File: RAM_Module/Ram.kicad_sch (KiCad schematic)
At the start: 3 parts, among them SW1 SW_Push, U3 74LS157, U4 74LS00

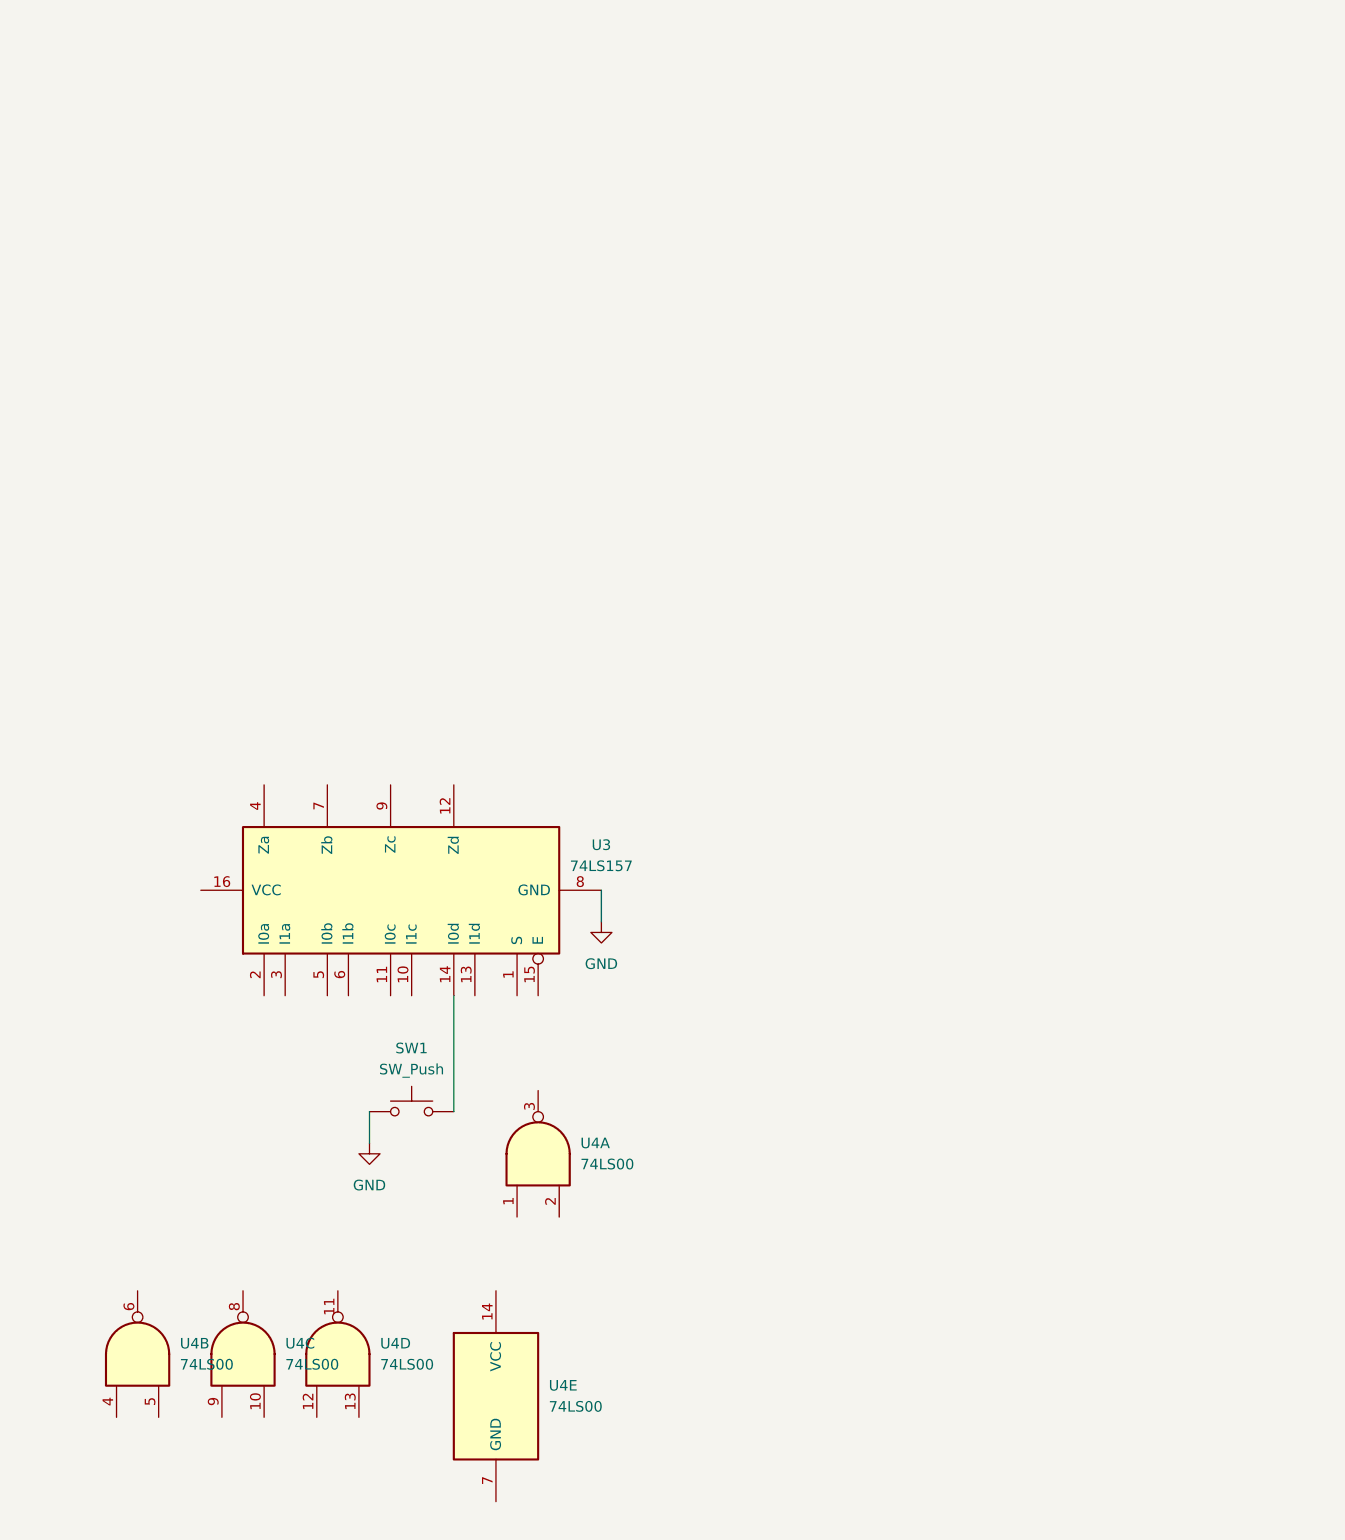
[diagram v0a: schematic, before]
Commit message: added buses for addresses. RAM WIP
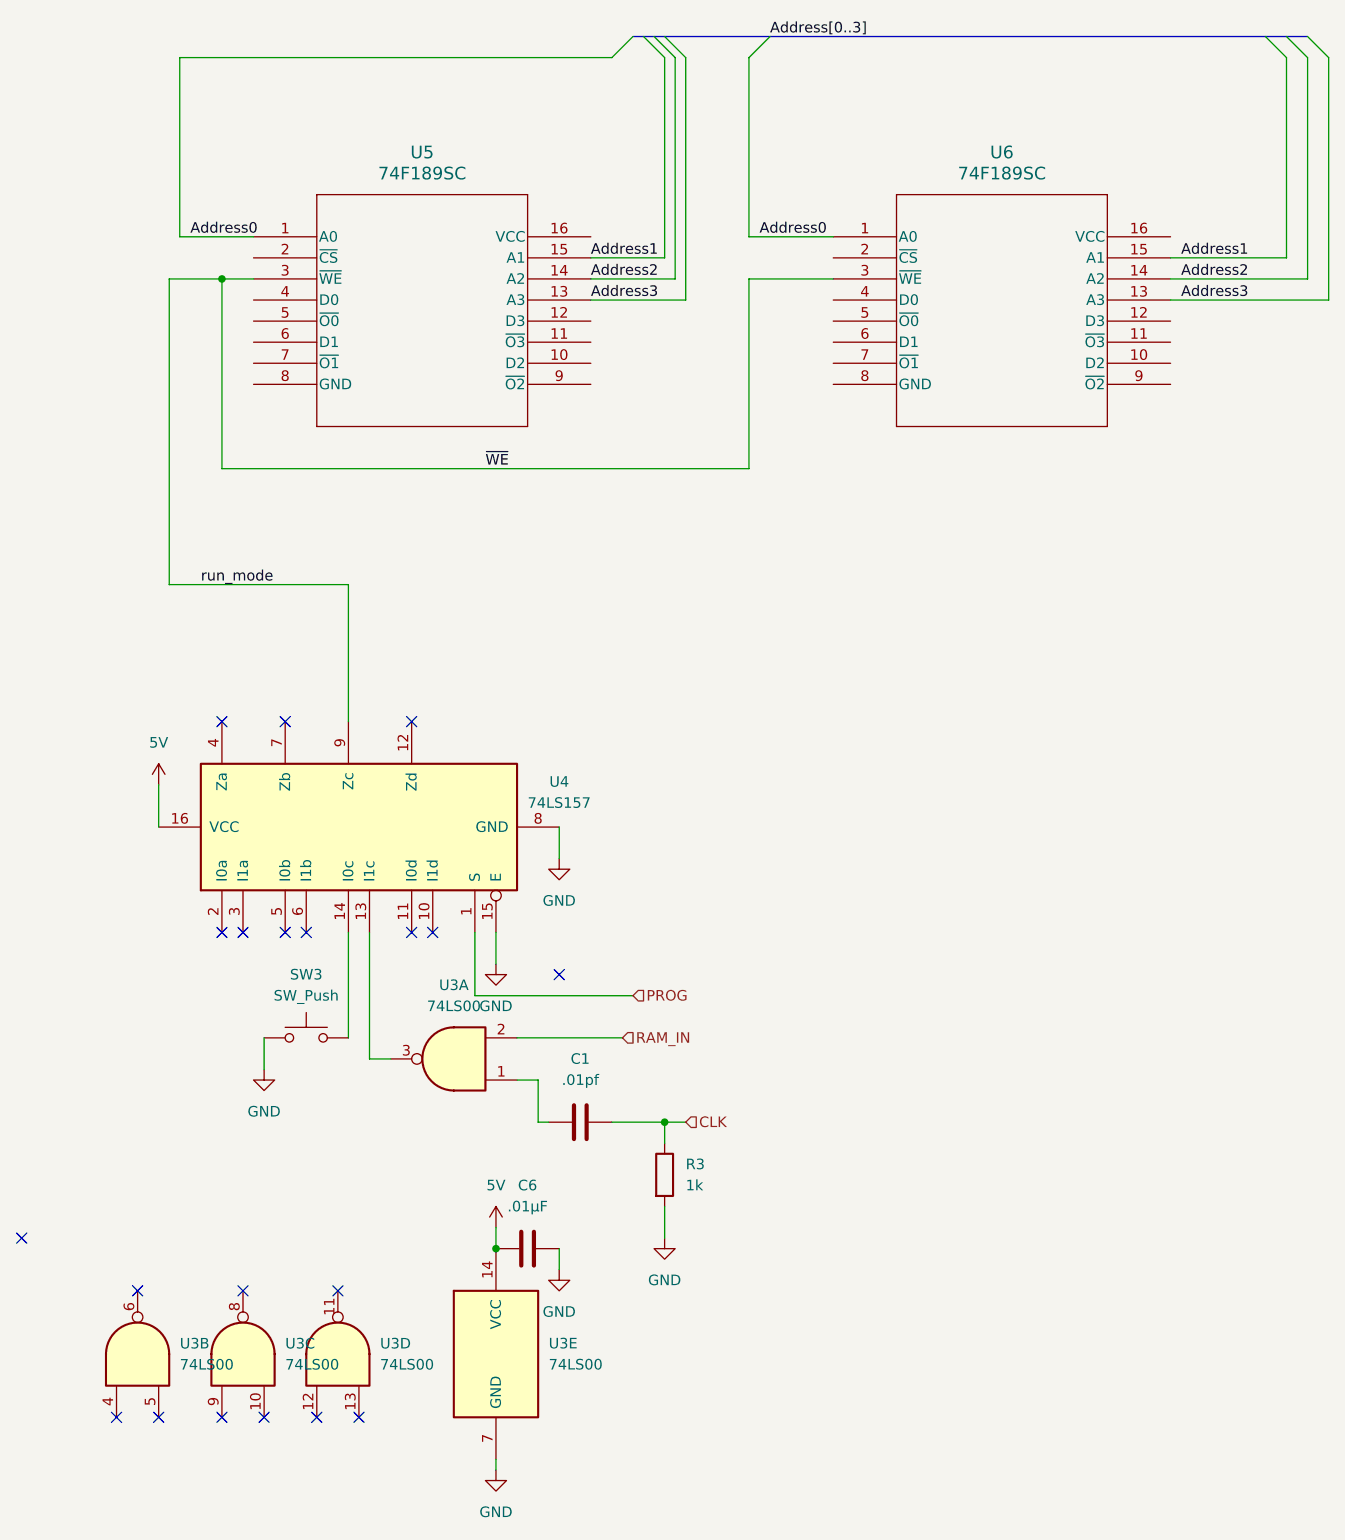
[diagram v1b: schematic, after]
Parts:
- added C1: .01pf, symbol Device:C
- added C6: .01µF, Capacitor_THT:C_Disc_D5.0mm_W2.5mm_P2.50mm, symbol Device:C
- added R3: 1k, symbol Device:R
- added U5, U6: 74F189SC, SOIC16_9P9X3P9_ONS, symbol 74189:74F189SC
- U4: renamed from U3; symbol 74xx:74LS157 -> 74LS157:my_74LS157
- renumbered SW1 to SW3, U4 to U3
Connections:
- net GND: now also U3.7 (GND), U4.15 (E), C6.1, R3.2
- net 5V: now reaches U3.14 (VCC)
- net 5V: now also U4.16 (VCC), C6.2
- net PROG: now reaches U4.1 (S)
- net at U4.13 (I1c): now also U3.3
- net run_mode: now reaches U4.9 (Zc)
- net run_mode: now also U5.3 (~{WE}), U6.3 (~{WE})
- net at U3.1: now also C1.1
- net RAM_IN: now reaches U3.2
- new net Address0: U5.1 (A0), U6.1 (A0)
- new net Address1: U5.15 (A1), U6.15 (A1)
- new net Address2: U5.14 (A2), U6.14 (A2)
- new net Address3: U5.13 (A3), U6.13 (A3)
- new net CLK: C1.2, R3.1
- no-connect marks 0 -> 20
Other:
- moved on the sheet: SW3, U3A, U3E, U4

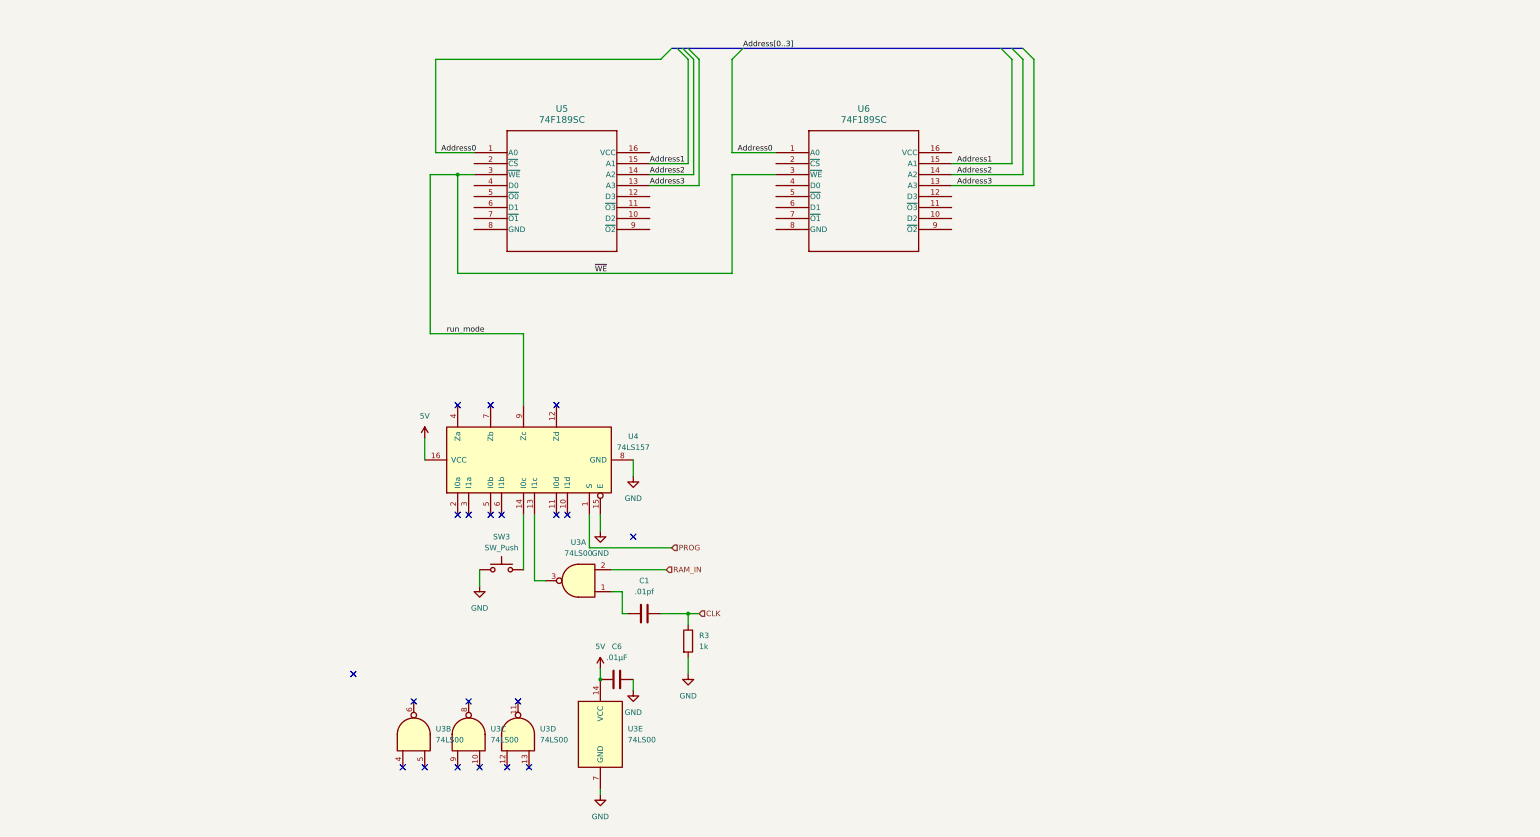
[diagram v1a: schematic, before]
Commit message: connected internal memory
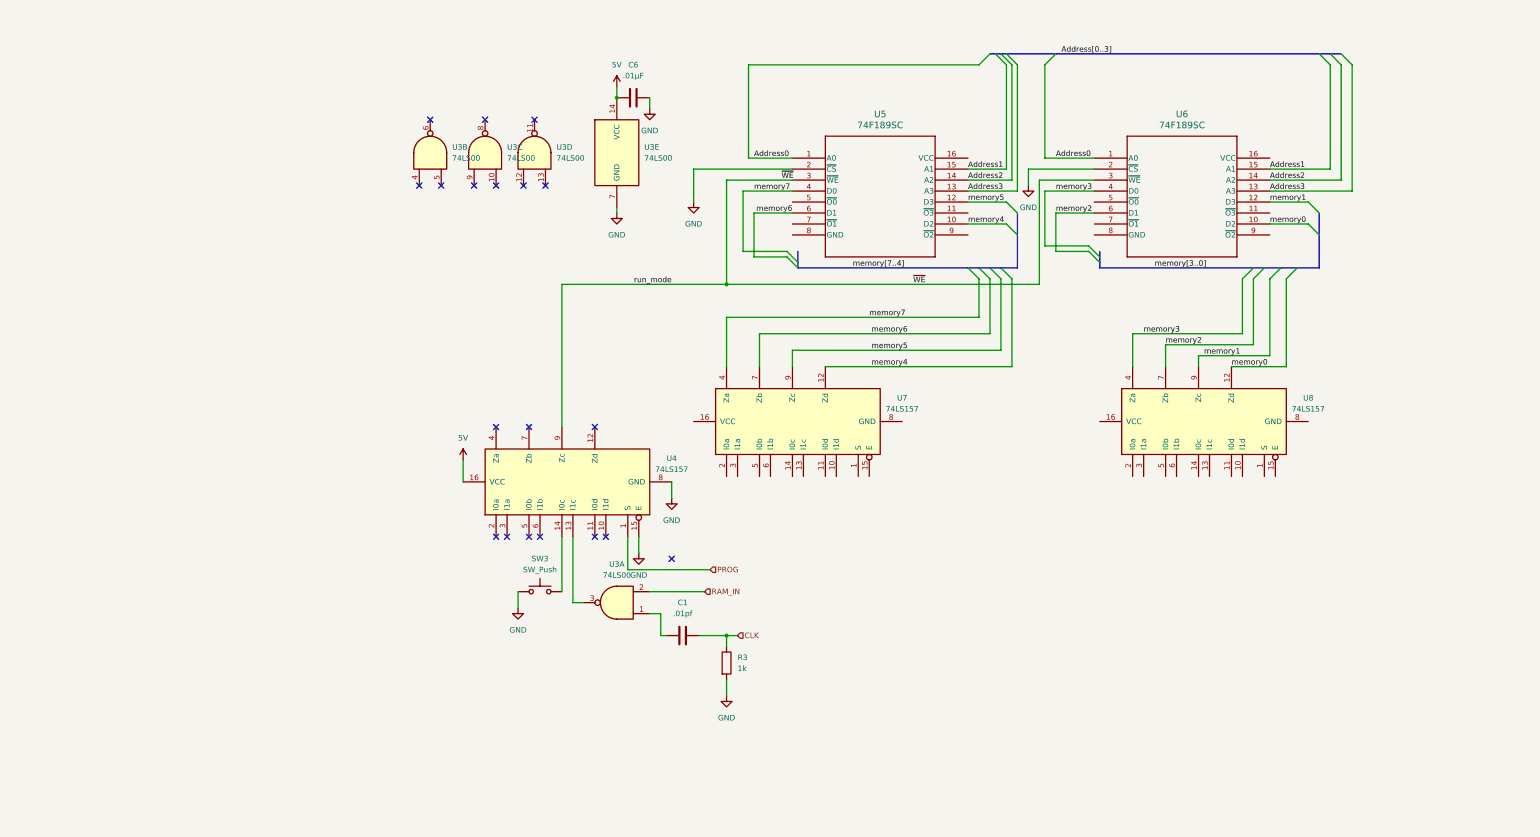
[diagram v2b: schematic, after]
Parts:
- added U7, U8: 74LS157, symbol 74LS157:my_74LS157
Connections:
- net GND: now also U5.2 (~{CS}), U6.2 (~{CS})
- net memory4: now reaches U5.10 (D2)
- net memory4: now also U7.12 (Zd)
- net memory5: now reaches U5.12 (D3)
- net memory5: now also U7.9 (Zc)
- net memory7: now reaches U5.4 (D0)
- net memory7: now also U7.4 (Za)
- net memory6: now reaches U5.6 (D1)
- net memory6: now also U7.7 (Zb)
- net memory0: now reaches U6.10 (D2)
- net memory0: now also U8.12 (Zd)
- net memory1: now reaches U6.12 (D3)
- net memory1: now also U8.9 (Zc)
- net memory3: now reaches U6.4 (D0)
- net memory3: now also U8.4 (Za)
- net memory2: now reaches U6.6 (D1)
- net memory2: now also U8.7 (Zb)
- no-connect marks 20 -> 19
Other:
- moved on the sheet: C1, C6, R3, SW3, U3A, U3B, U3C, U3D, U3E, U4, U5, U6
